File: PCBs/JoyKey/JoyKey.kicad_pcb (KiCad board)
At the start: 2 copper layers, 100 x 56.8 mm, 55 parts, among them J1 OLED_DISPLAY, J2 Conn_01x03_Socket, J3 Testpad wire hole1, J4 JST PH, J5 Top Trigger 1, J6 Top Trigger 2, Q1 PMOS,Si7157DP, SW1 RotaryEncoder_Switch, SW2 SW_Push_45deg, SW3 SW_Push_45deg, SW4 SW_Push_45deg, SW5 SW_Push_45deg, SW6 SW_Push_45deg, SW7 SW_Push_45deg, U1 BQ25060, U2 LSM6DSL, U3 XIAO-RP2040-DIP, U4 LP2981-3.3, U5 2_axis_analog_joystick_button

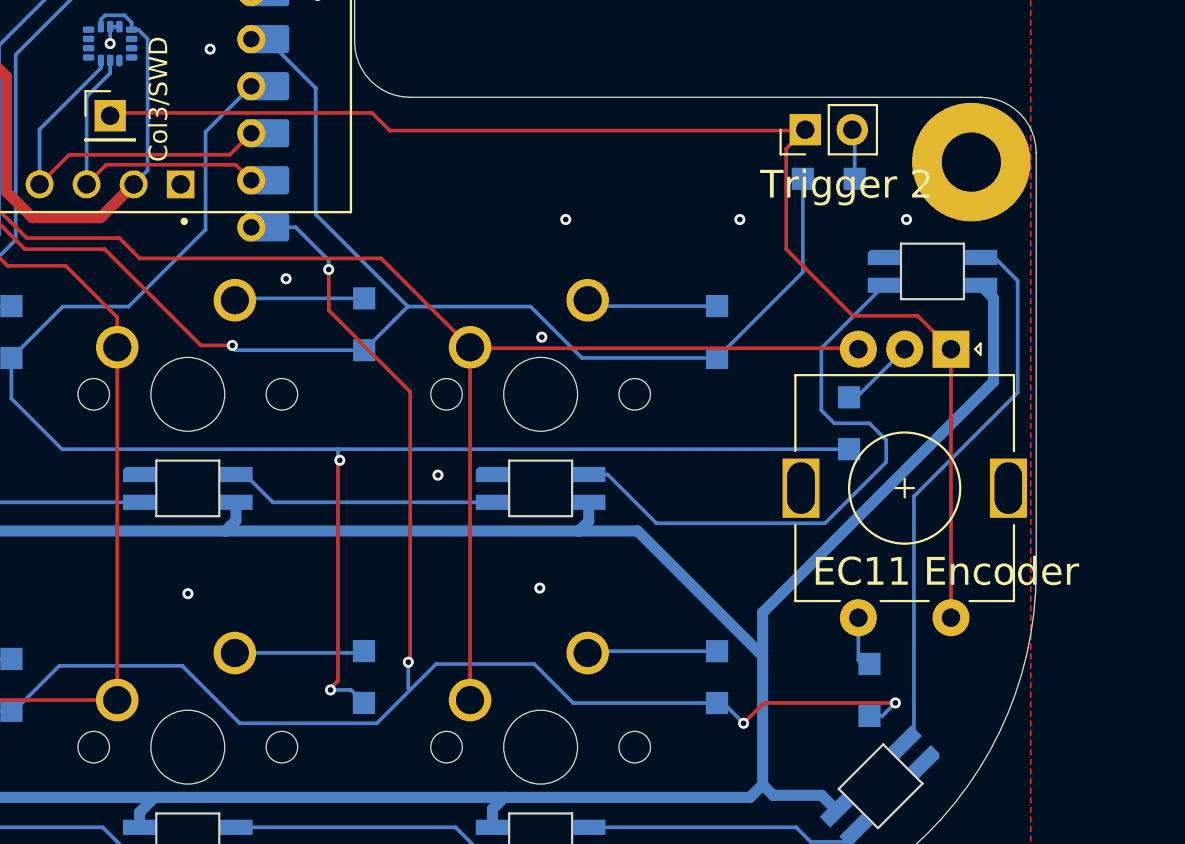
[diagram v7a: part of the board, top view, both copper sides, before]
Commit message: Switched encoder to Alps EC12
I wanted something shorter and that didn't have a metal screw post. I do loose out on the switch though, which I've exposed via a separate header
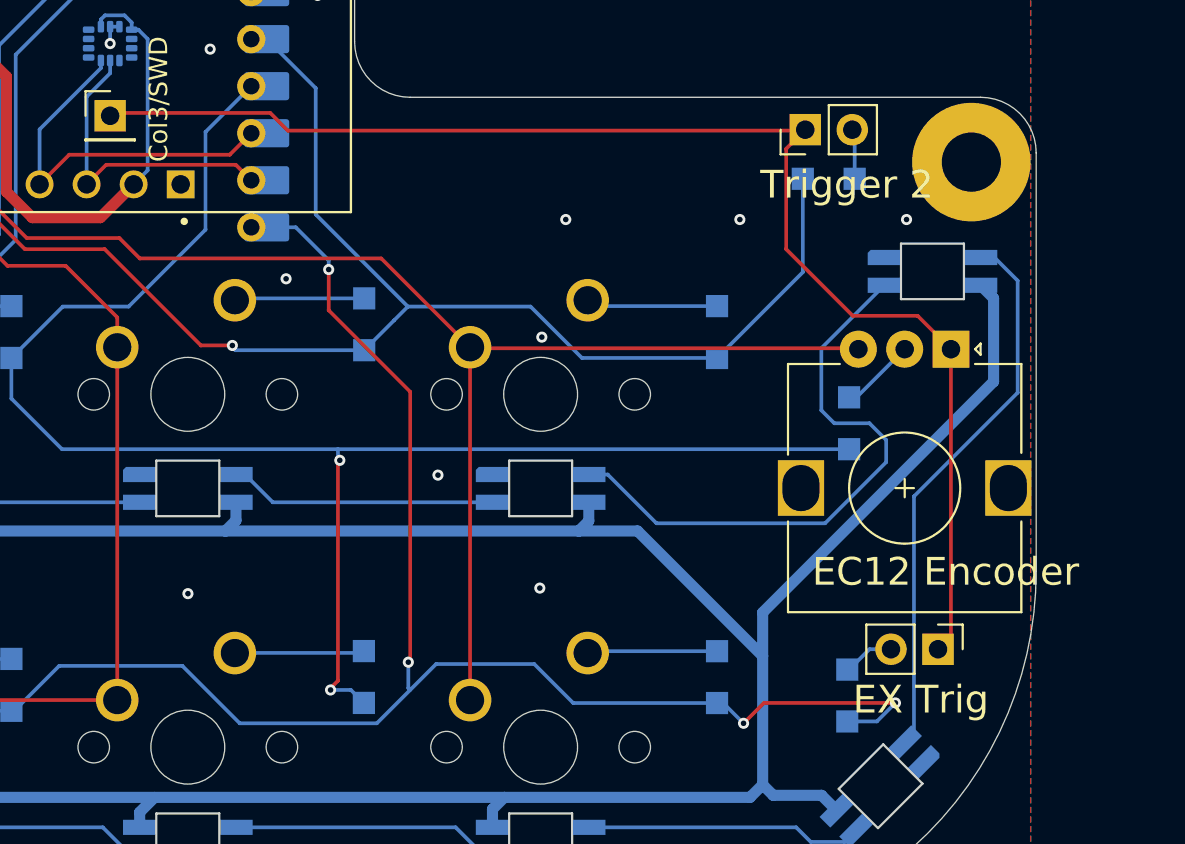
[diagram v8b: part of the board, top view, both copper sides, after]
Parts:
- added J7: Extra Trigger, Connector_PinHeader_2.54mm:PinHeader_1x02_P2.54mm_Vertical, F.Cu at (181.0, 123.3)
- SW1: footprint Rotary_Encoder:RotaryEncoder_Alps_EC11E-Switch_Vertical_H20mm -> Rotary_Encoder:RotaryEncoder_Alps_EC12E_Vertical_H20mm
- moved D17 1.24 mm to (176.1, 125.8)
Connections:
- D17 pad 2: /Analog Input/EC11SWB -> Net-(D17-A)
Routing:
- net /Analog Input/EC11SWB: track 2.98 -> 0.00 mm
- net Net-(D17-A): track 0.00 -> 2.82 mm
- net /COL3: track 70.5 -> 72.5 mm
- net /ROW2: track 125.0 -> 126.3 mm
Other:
- board text added: "EC12 Encoder"
- board text added: "EX Trig"
- board text removed: "EC11 Encoder"
